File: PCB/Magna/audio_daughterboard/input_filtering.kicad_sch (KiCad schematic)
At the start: 23 parts, among them U1001 NE5532, U1002 NE5532, U1003 LM1971M

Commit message: Add simulation to all components
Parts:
- removed C1006, C1007: 100nF/50V, Capacitor_SMD:C_0805_2012Metric_Pad1.18x1.45mm_HandSolder, symbol Device:C
- removed RV1001: 2k, symbol Device:R_Potentiometer
- added C101, C102: 100nF, Capacitor_SMD:C_0805_2012Metric_Pad1.18x1.45mm_HandSolder, symbol Device:C
- added C103, C105, C106, C107, C108, C109: 1000p, symbol Device:C
- added R101, R104: 3920, symbol Device:R
- added R102, R106, R107, R111: 7320, symbol Device:R
- added R103, R108: 3480, symbol Device:R
- added R105, R109: 1330, symbol Device:R
- added U101, U102, U103: NE5532, symbol Amplifier_Operational:NE5532
- added V101: 14, symbol Simulation_SPICE:VDC
- added V102: VSIN, symbol Simulation_SPICE:VSIN
- added V103: 7, symbol Simulation_SPICE:VDC
- C1008: value 100nF/50V -> 100nF; Voltage (none) -> 50V
- U1003: Availability In Stock -> (none); Check_prices https://www.snapeda.com/parts/LM1971MX/Texas+Instruments/vi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 -> (none); Purchase-URL https://www.snapeda.com/api/url_track_click_mouser/?unipart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 -> (none); SnapEDA_Link https://www.snapeda.com/parts/LM1971MX/Texas+Instruments/vi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 -> (none)
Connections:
- net GND: now also C101.2, C102.2, C105.2, C107.2, C108.2, C109.2, U101.4 (V-), U102.4 (V-), U103.4 (V-), V101.2, V102.2, V103.2
- net VAA: now also C101.1, C102.1, U101.8 (V+), U102.8 (V+), U103.8 (V+), V101.1
- net V_bias: now also V103.1
- net signal in: now also V102.1
- net at R1008.2, TP1003.1, U1002.7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: now also TP1002.1, U1003.2 (OUT)
- net at C1004.2, R1007.1, U1001.7: now also U1001.6 (-); no longer U1001.5 (+)
- net at C1002.2, R1003.1, TP1001.1: now also U1001.3 (+); no longer U1001.2 (-)
- net at C1005.1, R1006.2: now also U1001.5 (+); no longer U1001.6 (-)
- net at R1004.2, U1001.1: now also U1001.2 (-), R101.1; no longer U1001.3 (+)
- new net: C103.2, R103.2, U101.1
- new net: C103.1, R111.1, U101.2 (-), U101.6 (-)
- new net: R101.2, R102.2, R105.2, U101.3 (+)
- new net: C108.1, R109.1, U103.5 (+)
- new net: C106.1, R107.1, U102.6 (-), U103.2 (-)
- new net: R106.1, R107.2, U102.7
- new net: R104.2, R106.2, R109.2, U103.3 (+)
- new net: C107.1, R108.1, U102.5 (+)
- new net: R102.1, R111.2, U101.7
- new net: R104.1, U102.1, U102.2 (-)
- new net: C105.1, R105.1, U102.3 (+)
- new net: C109.1, R103.1, U101.5 (+)
- new net: C106.2, R108.2, U103.1
- new net six_pole: U103.6 (-), U103.7
- now unconnected: U1002.3 (+)
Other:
- note added: ".ac dec 100 5 500k"
- moved on the sheet: U1002A

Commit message: Finish simulations and design of input filtering
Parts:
- removed C1003, C1004: 33nF, symbol Device:C
- removed C1005: 4.7nF, symbol Device:C
- removed C102: 100nF, Capacitor_SMD:C_0805_2012Metric_Pad1.18x1.45mm_HandSolder, symbol Device:C
- removed R1004: 130R, symbol Device:R
- removed R1005: 430R, symbol Device:R
- removed R1006: 220R, symbol Device:R
- removed U1002: NE5532, symbol Amplifier_Operational:NE5532
- added C1007, C1010, C1012: 100nF, Capacitor_SMD:C_0805_2012Metric_Pad1.18x1.45mm_HandSolder, symbol Device:C
- added R1002: 11k, symbol Device:R
- added R1003: 1k, symbol Device:R
- added S1001: SWITCH, symbol Simulation_SPICE:SWITCH
- R1016: renamed from R1007; value 1k -> 180
- R1017: renamed from R1008; value 1k -> 390
- renumbered C103 to C1003, C109 to C1004, C105 to C1005, C101 to C1006, C106 to C1008, C107 to C1009, C108 to C1011, C1008 to C1013, R1002 to R1004, R1003 to R1005, R101 to R1006, R102 to R1007, R111 to R1008, R103 to R1009, R105 to R1010, R104 to R1011, R106 to R1012, R107 to R1013, R108 to R1014, R109 to R1015, U101 to U1002, U102 to U1003, U103 to U1004, U1003 to U1005, V102 to V1001, V103 to V1002, V101 to V1003
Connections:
- net GND: now also C1007.2, C1010.2, C1012.2, S1001.4 (C-)
- net VAA: now also C1007.1, C1010.1, C1012.1, S1001.3 (C+)
- net V_bias: now also R1016.1, R1003.2
- net signal_out: now also R1017.2, TP1003.1, U1001.7
- net at R1016.2, R1017.1: now also U1001.6 (-)
- net input_biased: now reaches C1002.2, R1005.1, TP1001.1, U1001.3 (+)
- net antennuated_input: now reaches U1001.5 (+)
- net antennuated_input: now also TP1002.1, U1005.2 (OUT), R1002.2, R1003.1
- net six_pole renamed Filtered_input
- net Filtered_input: now also U1005.8 (IN), R1002.1, S1001.1 (N+)
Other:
- note added: ".ac dec 100 5 500k .ic V(/input_biased)=7"
- note added: "6Pole lowpass filter (40kHz)"
- note added: "Input filter"
- note removed: ".ac dec 100 5 500k"
- note removed: "Sallen Key low pass filter Cutoff 40KHz"
- moved on the sheet: C1001, C1002, C1003, C1004, C1005, C1006, C1008, C1009, C1011, C1013, R1001, R1004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

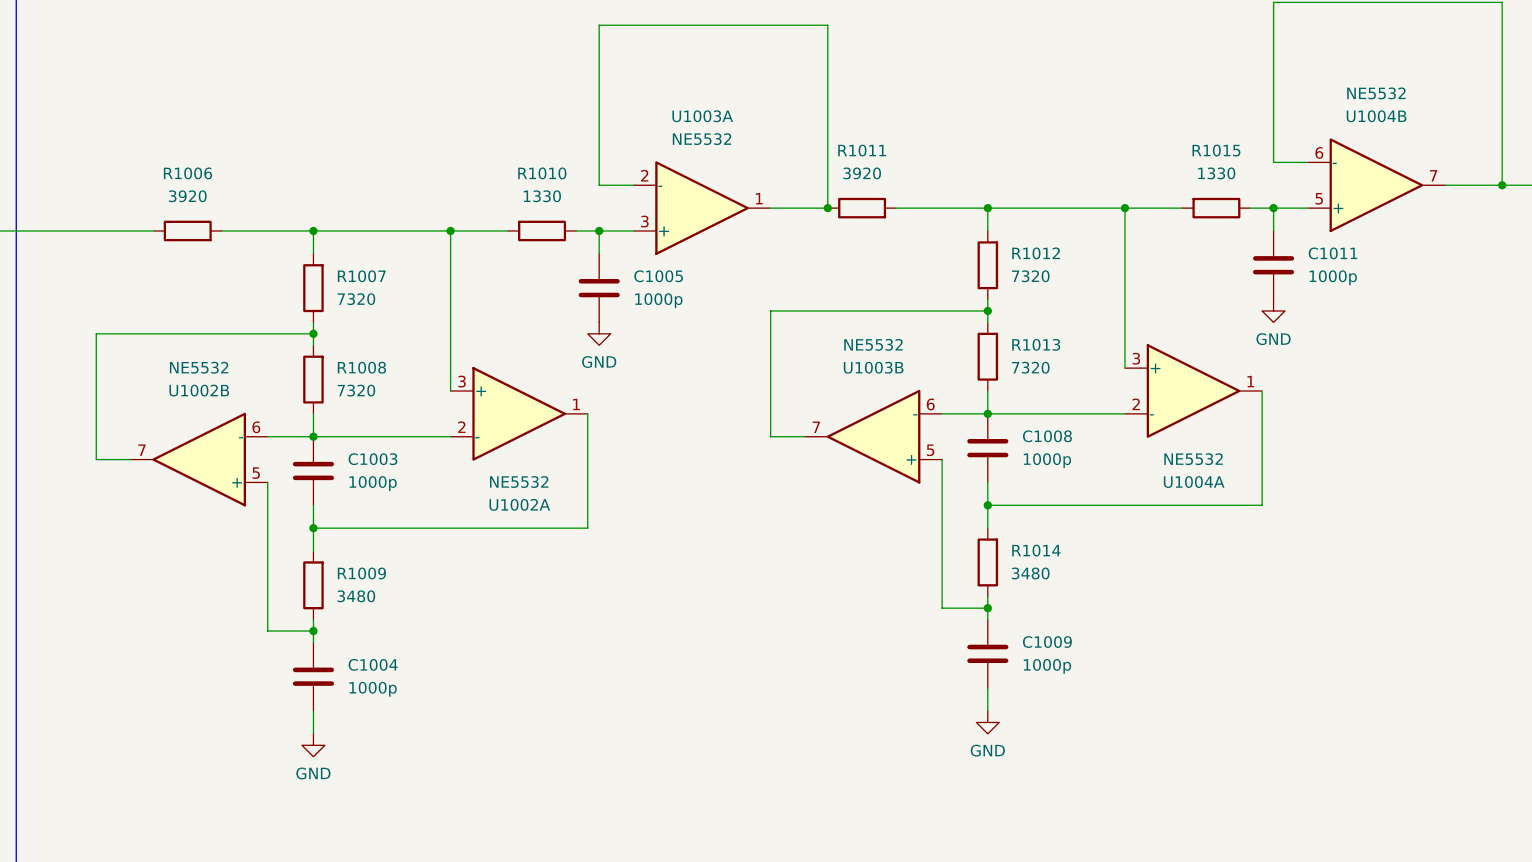
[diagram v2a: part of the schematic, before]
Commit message: Change ADC and add MCU for IO control
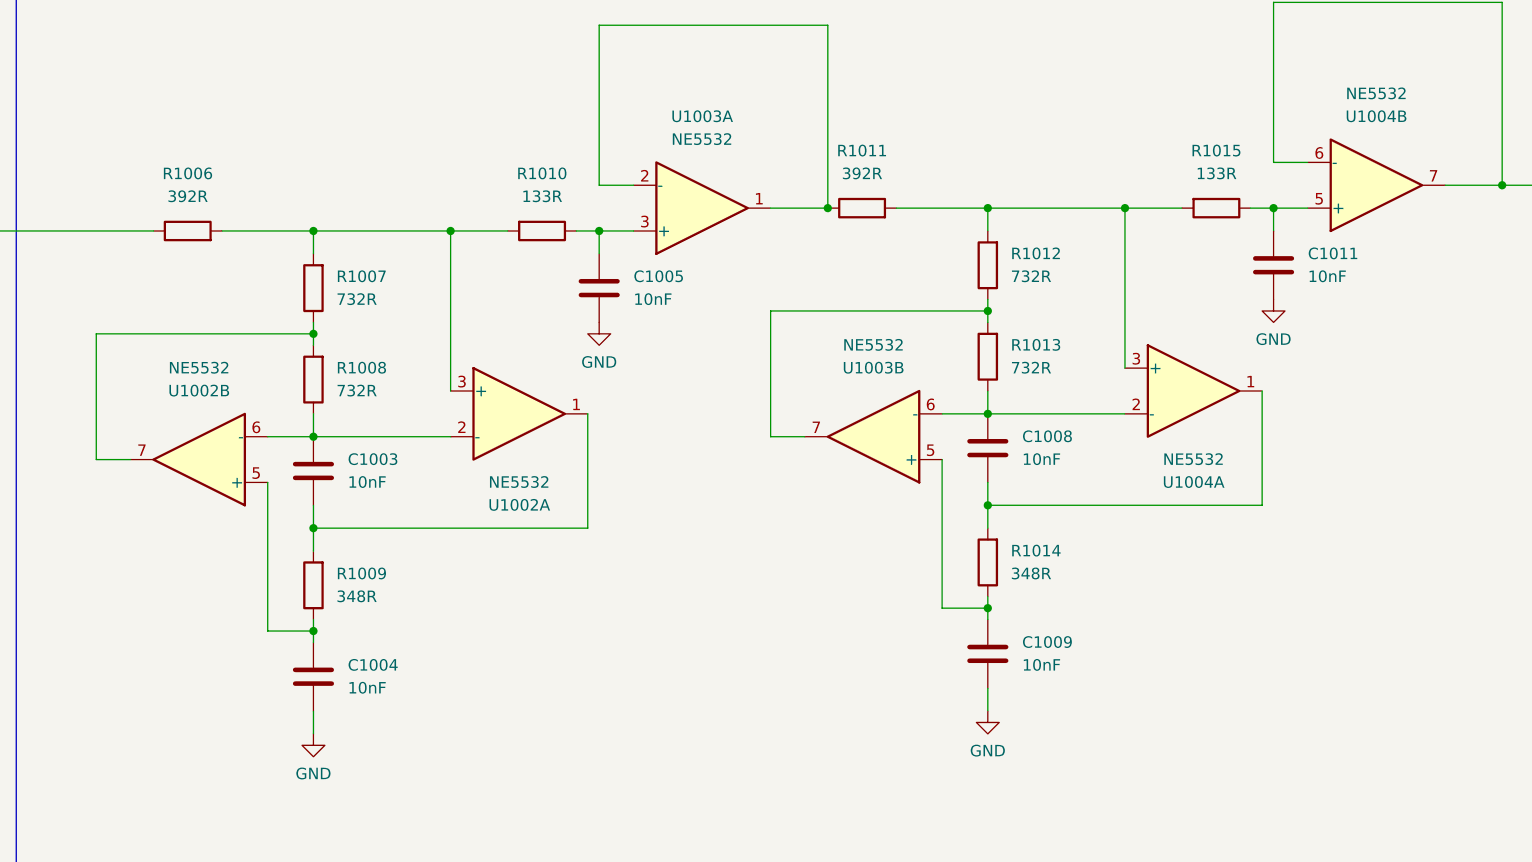
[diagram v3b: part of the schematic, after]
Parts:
- C1003, C1004, C1005, C1008, C1009, C1011: value 1000p -> 10nF
- R1006, R1011: value 3920 -> 392R
- R1007, R1008, R1012, R1013: value 7320 -> 732R
- R1009, R1014: value 3480 -> 348R
- R1010, R1015: value 1330 -> 133R

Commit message: Update schematics to Kicad 9
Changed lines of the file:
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@@
 					(size 1.27 1.27)
 				)
+				(hide yes)
 			)
 		)
@@
 					(size 1.27 1.27)
 				)
+				(hide yes)
 			)
 		)
@@
 					(size 1.27 1.27)
 				)
+				(hide yes)
 			)
 		)
@@
 					(size 1.27 1.27)
 				)
+				(hide yes)
 			)
 		)
@@
 					(size 1.27 1.27)
 				)
+				(hide yes)
 			)
 		)
@@
 					(size 1.27 1.27)
 				)
+				(hide yes)
 			)
 		)
@@
 					(size 1.27 1.27)
 				)
+				(hide yes)
 			)
 		)
@@
 					(size 1.27 1.27)
 				)
+				(hide yes)
 			)
 		)
@@
 					(size 1.27 1.27)
 				)
+				(hide yes)
 			)
 		)
@@
 					(size 1.27 1.27)
 				)
+				(hide yes)
 			)
 		)
@@
 					(size 1.27 1.27)
 				)
+				(hide yes)
 			)
 		)
@@
 					(size 1.27 1.27)
 				)
+				(hide yes)
 			)
 		)
@@
 					(size 1.27 1.27)
 				)
+				(hide yes)
 			)
 		)
@@
 					(size 1.27 1.27)
 				)
+				(hide yes)
 			)
 		)
@@
 					(size 1.27 1.27)
 				)
+				(hide yes)
 			)
 		)
@@
 					(size 1.27 1.27)
 				)
+				(hide yes)
 			)
 		)
@@
 					(size 1.27 1.27)
 				)
+				(hide yes)
 			)
 		)
@@
 					(size 1.27 1.27)
 				)
+				(hide yes)
 			)
 		)
@@
 					(size 1.27 1.27)
 				)
+				(hide yes)
 			)
 		)
@@
 					(size 1.27 1.27)
 				)
+				(hide yes)
 			)
 		)
@@
 					(size 1.27 1.27)
 				)
+				(hide yes)
 			)
 		)
@@
 					(size 1.27 1.27)
 				)
+				(hide yes)
 			)
 		)
@@
 					(size 1.27 1.27)
 				)
+				(hide yes)
 			)
 		)
@@
 					(size 1.27 1.27)
 				)
+				(hide yes)
 			)
 		)
@@
 					(size 1.27 1.27)
 				)
+				(hide yes)
 			)
 		)
@@
 					(size 1.27 1.27)
 				)
+				(hide yes)
 			)
 		)
@@
 					(size 1.27 1.27)
 				)
+				(hide yes)
 			)
 		)
@@
 					(size 1.27 1.27)
 				)
+				(hide yes)
 			)
 		)
@@
 					(size 1.27 1.27)
 				)
+				(hide yes)
 			)
 		)
@@
 					(size 1.27 1.27)
 				)
+				(hide yes)
 			)
 		)
@@
 					(size 1.27 1.27)
 				)
+				(hide yes)
 			)
 		)
@@
 					(size 1.27 1.27)
 				)
+				(hide yes)
 			)
 		)
@@
 					(size 1.27 1.27)
 				)
+				(hide yes)
 			)
 		)
@@
 					(size 1.27 1.27)
 				)
+				(hide yes)
 			)
 		)
@@
 					(size 1.27 1.27)
 				)
+				(hide yes)
 			)
 		)
@@
 					(size 1.27 1.27)
 				)
+				(hide yes)
 			)
 		)
@@
 					(size 1.27 1.27)
 				)
+				(hide yes)
 			)
 		)
@@
 					(size 1.27 1.27)
 				)
+				(hide yes)
 			)
 		)
@@
 					(size 1.27 1.27)
 				)
+				(hide yes)
 			)
 		)
@@
 					(size 1.27 1.27)
 				)
+				(hide yes)
 			)
 		)
@@
 					(size 1.27 1.27)
 				)
+				(hide yes)
 			)
 		)
@@
 					(size 1.27 1.27)
 				)
+				(hide yes)
 			)
 		)
@@
 					(size 1.27 1.27)
 				)
+				(hide yes)
 			)
 		)
@@
 					(size 1.27 1.27)
 				)
+				(hide yes)
 			)
 		)
@@
 					(size 1.27 1.27)
 				)
+				(hide yes)
 			)
 		)
@@
 					(size 1.27 1.27)
 				)
+				(hide yes)
 			)
 		)
@@
 				)
 				(justify left)
+				(hide yes)
 			)
 		)
@@
 					(size 1.27 1.27)
 				)
+				(hide yes)
 			)
 		)
@@
 					(size 1.27 1.27)
 				)
+				(hide yes)
 			)
 		)
@@
 					(size 1.27 1.27)
 				)
+				(hide yes)
 			)
 		)
@@
 					(size 1.27 1.27)
 				)
+				(hide yes)
 			)
 		)
@@
 					(size 1.27 1.27)
 				)
+				(hide yes)
 			)
 		)
@@
 					(size 1.27 1.27)
 				)
+				(hide yes)
 			)
 		)
@@
 					(size 1.27 1.27)
 				)
+				(hide yes)
 			)
 		)
@@
 					(size 1.27 1.27)
 				)
+				(hide yes)
 			)
 		)
@@
 					(size 1.27 1.27)
 				)
+				(hide yes)
 			)
 		)
@@
 				)
 				(justify left)
+				(hide yes)
 			)
 		)
@@
 					(size 1.27 1.27)
 				)
+				(hide yes)
 			)
 		)
@@
 					(size 1.27 1.27)
 				)
+				(hide yes)
 			)
 		)
@@
 					(size 1.27 1.27)
 				)
+				(hide yes)
 			)
 		)
@@
 					(size 1.27 1.27)
 				)
+				(hide yes)
 			)
 		)
@@
 					(size 1.27 1.27)
 				)
+				(hide yes)
 			)
 		)
@@
 					(size 1.27 1.27)
 				)
+				(hide yes)
 			)
 		)
@@
 					(size 1.27 1.27)
 				)
+				(hide yes)
 			)
 		)
@@
 					(size 1.27 1.27)
 				)
+				(hide yes)
 			)
 		)
@@
 					(size 1.27 1.27)
 				)
+				(hide yes)
 			)
 		)
@@
 					(size 1.27 1.27)
 				)
+				(hide yes)
 			)
 		)
@@
 					(size 1.27 1.27)
 				)
+				(hide yes)
 			)
 		)
@@
 					(size 1.27 1.27)
 				)
+				(hide yes)
 			)
 		)
@@
 					(size 1.27 1.27)
 				)
+				(hide yes)
 			)
 		)

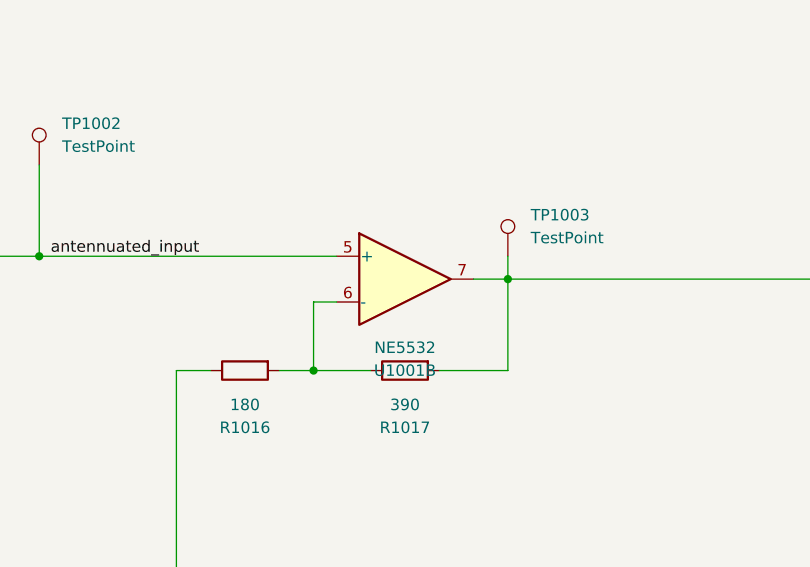
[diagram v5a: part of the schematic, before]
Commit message: Update audio PCB
Mainly added simulations to Linedriver and DAC.

Also fixed some small issues that was found when simulating
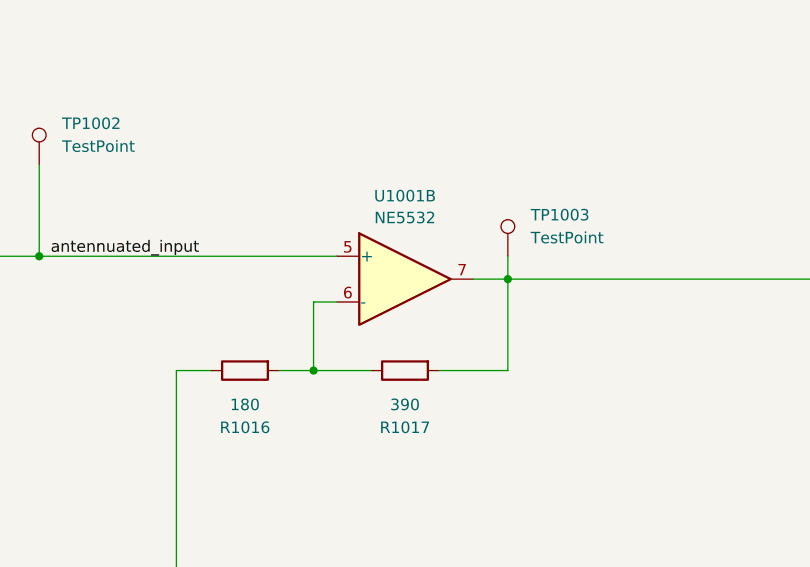
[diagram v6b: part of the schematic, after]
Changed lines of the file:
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@@
 		(on_board yes)
 		(dnp no)
+		(fields_autoplaced yes)
 		(property "Reference" "U1001"
-			(at 481.33 82.55 0)
+			(at 481.33 63.1655 0)
 			(effects
 				(font
@@
 		)
 		(property "Value" "NE5532"
-			(at 481.33 80.01 0)
+			(at 481.33 65.5898 0)
 			(effects
 				(font

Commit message: "Finalize" Audio daugherboard
Finished DAC output filter
Fixed the whole damn MCU subschematic
Fixed Linedriver schematic
Added component footprints and LCSC numbers
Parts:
- removed R1016: 180, symbol Device:R
- added R1006: 100k, Resistor_SMD:R_0603_1608Metric, symbol Device:R
- added R1018: 2k15, Resistor_SMD:R_0603_1608Metric, symbol Device:R
- C1001: value 220pF -> 390pF; footprint (none) -> Capacitor_SMD:C_0603_1608Metric; LCSC (none) -> C472793; now left out of the parts list
- C1002: footprint (none) -> Skrooter_footprints:c_elec_SMD_12.5x13.5; LCSC (none) -> C3829328; now left out of the parts list
- C1003, C1004, C1005, C1008, C1009, C1011: footprint (none) -> Capacitor_SMD:C_0603_1608Metric; LCSC (none) -> C84709; now left out of the parts list
- C1006, C1007, C1010, C1012, C1013, TP1001, TP1002, TP1003, V1001, V1002: now left out of the parts list
- R1001: footprint (none) -> Resistor_SMD:R_0603_1608Metric; LCSC (none) -> C122970; now left out of the parts list
- R1004: footprint (none) -> Resistor_SMD:R_0603_1608Metric; LCSC (none) -> C25803; now left out of the parts list
- R1005: value 47k -> 100k; footprint (none) -> Resistor_SMD:R_0603_1608Metric; LCSC (none) -> C25803; now left out of the parts list
- R1007: renamed from R1006; footprint (none) -> Resistor_SMD:R_0603_1608Metric; LCSC (none) -> C861870; now left out of the parts list
- R1008: renamed from R1007; footprint (none) -> Resistor_SMD:R_0603_1608Metric; LCSC (none) -> C861547; now left out of the parts list
- R1009: renamed from R1008; footprint (none) -> Resistor_SMD:R_0603_1608Metric; LCSC (none) -> C861547; now left out of the parts list
- R1010: renamed from R1009; footprint (none) -> Resistor_SMD:R_0603_1608Metric; LCSC (none) -> C861337; now left out of the parts list
- R1011: renamed from R1010; footprint (none) -> Resistor_SMD:R_0603_1608Metric; LCSC (none) -> C861112; now left out of the parts list
- R1012: renamed from R1011; footprint (none) -> Resistor_SMD:R_0603_1608Metric; LCSC (none) -> C861870; now left out of the parts list
- R1013: renamed from R1012; footprint (none) -> Resistor_SMD:R_0603_1608Metric; LCSC (none) -> C861547; now left out of the parts list
- R1014: renamed from R1013; footprint (none) -> Resistor_SMD:R_0603_1608Metric; LCSC (none) -> C861547; now left out of the parts list
- R1015: renamed from R1014; footprint (none) -> Resistor_SMD:R_0603_1608Metric; LCSC (none) -> C861337; now left out of the parts list
- R1016: renamed from R1015; footprint (none) -> Resistor_SMD:R_0603_1608Metric; LCSC (none) -> C861112; now left out of the parts list
- R1017: value 390 -> 1k; footprint (none) -> Resistor_SMD:R_0603_1608Metric; LCSC (none) -> C110776; now left out of the parts list
- S1001, V1003: now not fitted; now left out of the parts list
- U1001, U1002, U1003, U1004: footprint (none) -> Package_SO:SOIC-8_3.9x4.9mm_P1.27mm; LCSC (none) -> C7426; now left out of the parts list
- U1001: renamed from U1002; footprint (none) -> Package_SO:SOIC-8_3.9x4.9mm_P1.27mm; LCSC (none) -> C7426; now left out of the parts list
- U1002: renamed from U1003; footprint (none) -> Package_SO:SOIC-8_3.9x4.9mm_P1.27mm; LCSC (none) -> C7426; now left out of the parts list
- U1003: renamed from U1004; footprint (none) -> Package_SO:SOIC-8_3.9x4.9mm_P1.27mm; LCSC (none) -> C7426; now left out of the parts list
- U1004: renamed from U1001; footprint (none) -> Package_SO:SOIC-8_3.9x4.9mm_P1.27mm; LCSC (none) -> C7426; now left out of the parts list
- U1005: LCSC (none) -> C129348; now left out of the parts list
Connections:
- net GND: now also C1001.1; no longer C1001.2
- net V_bias: now also R1017.1, R1006.2
- net antennuated_input: now also S1001.2 (N-)
- net input_biased: now also C1002.1, R1006.1; no longer C1002.2
- net signal_out: now also R1018.2; no longer R1017.2
- net at U1004.6 (-): now also R1017.2, R1018.1; no longer R1017.1
- net input_filter: now reaches R1001.1, R1004.1
- net input_filter: now also C1001.2, C1002.2; no longer C1001.1, C1002.1
- net input_buffered: now reaches R1007.1, U1001.1, U1001.2 (-)
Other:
- moved on the sheet: C1003, C1004, C1008, C1009, R1010, R1015, TP1001, TP1003

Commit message: Do most of the component placement for audio board
Just a general layout, things will probably change
as the routing begins.
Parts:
- C1006, C1007, C1010, C1012, C1013: footprint Capacitor_SMD:C_0805_2012Metric_Pad1.18x1.45mm_HandSolder -> Capacitor_SMD:C_0603_1608Metric; LCSC C49678 -> C14663
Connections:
- net Filtered_input: now also U1004.5 (+), U1004.7; no longer U1003.6 (-), U1003.7
- net antennuated_input: now also U1004.3 (+); no longer U1004.5 (+)
- net signal_out: now also U1004.1; no longer U1004.7
- net at R1017.2, R1018.1: now also U1004.2 (-); no longer U1004.6 (-)
- net at C1011.1, R1016.1: now also U1004.6 (-); no longer U1003.5 (+)
- net at C1008.1, R1014.1: now also U1003.2 (-), U1003.5 (+); no longer U1002.6 (-), U1004.2 (-)
- net at R1013.1, R1014.2: now also U1003.1; no longer U1002.7
- net at R1012.2, R1013.2, R1016.2: now also U1003.6 (-); no longer U1004.3 (+)
- net at C1009.1, R1015.1: now also U1003.3 (+); no longer U1002.5 (+)
- net at C1005.1, R1011.1: now also U1002.5 (+); no longer U1003.3 (+)
- net at C1008.2, R1015.2: now also U1003.7; no longer U1004.1
- new net: R1012.1, U1002.6 (-), U1002.7
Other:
- moved on the sheet: U1002B, U1003A, U1003B, U1004A, U1004B
